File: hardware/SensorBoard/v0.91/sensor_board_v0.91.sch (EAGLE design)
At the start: 46 parts, among them IC1 BMP280, IC2 VREF, J3 USB-MICROB, U1 LMP91000, U10 CCS811, U11 RFM69HW, U2 TSL2561, U3 ATMEGA328P-MU, U4 ADS1115, U7 SHT31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

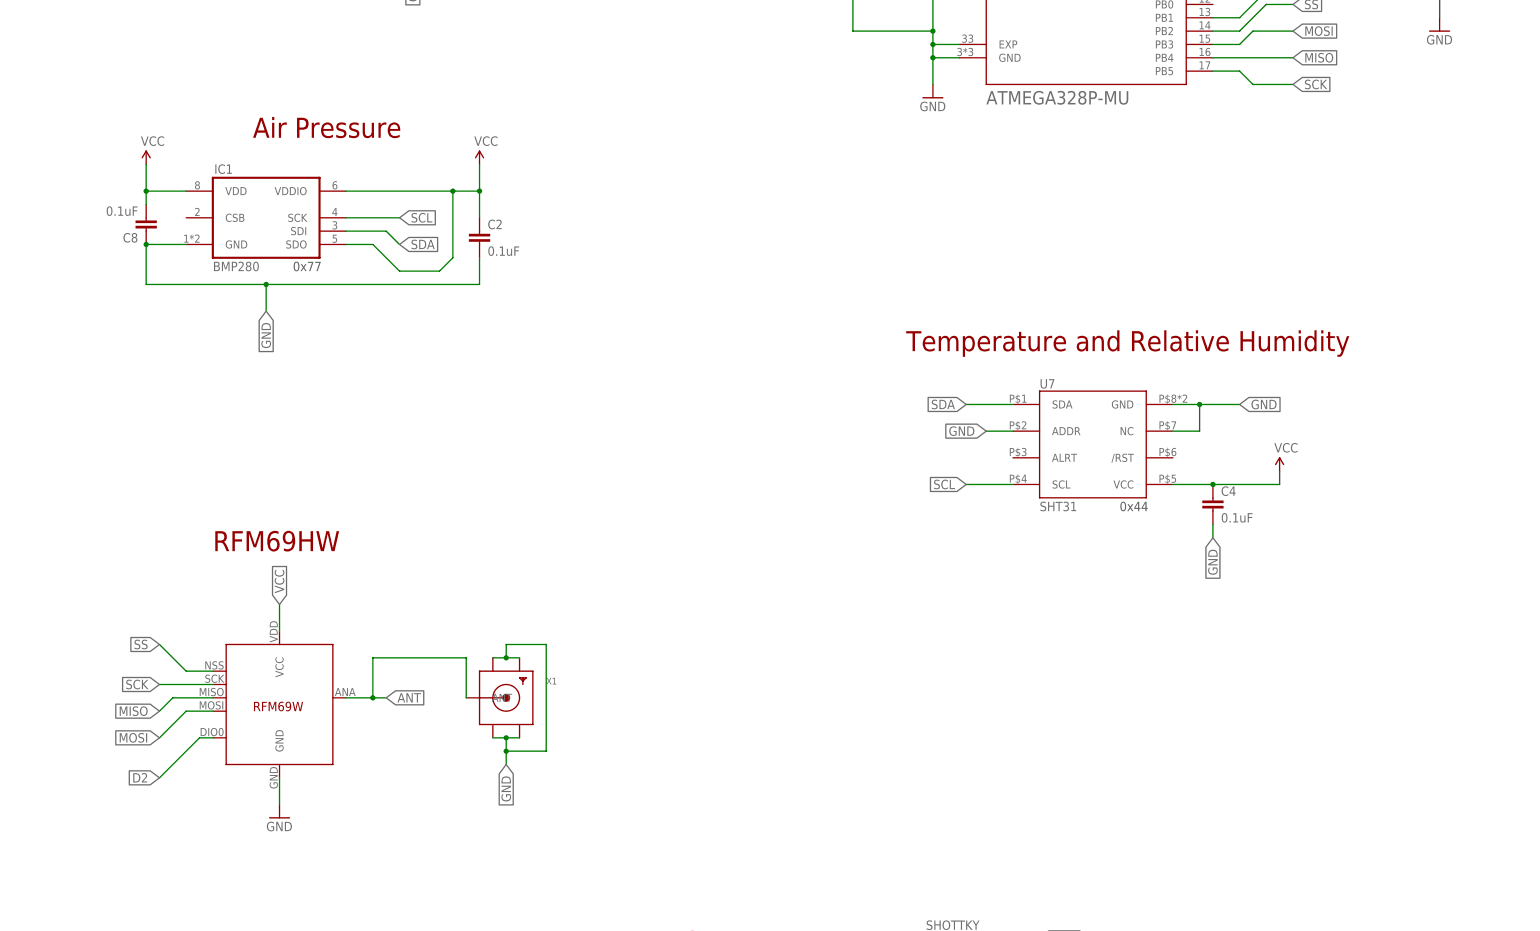
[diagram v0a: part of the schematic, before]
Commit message: Updated SHT31 library
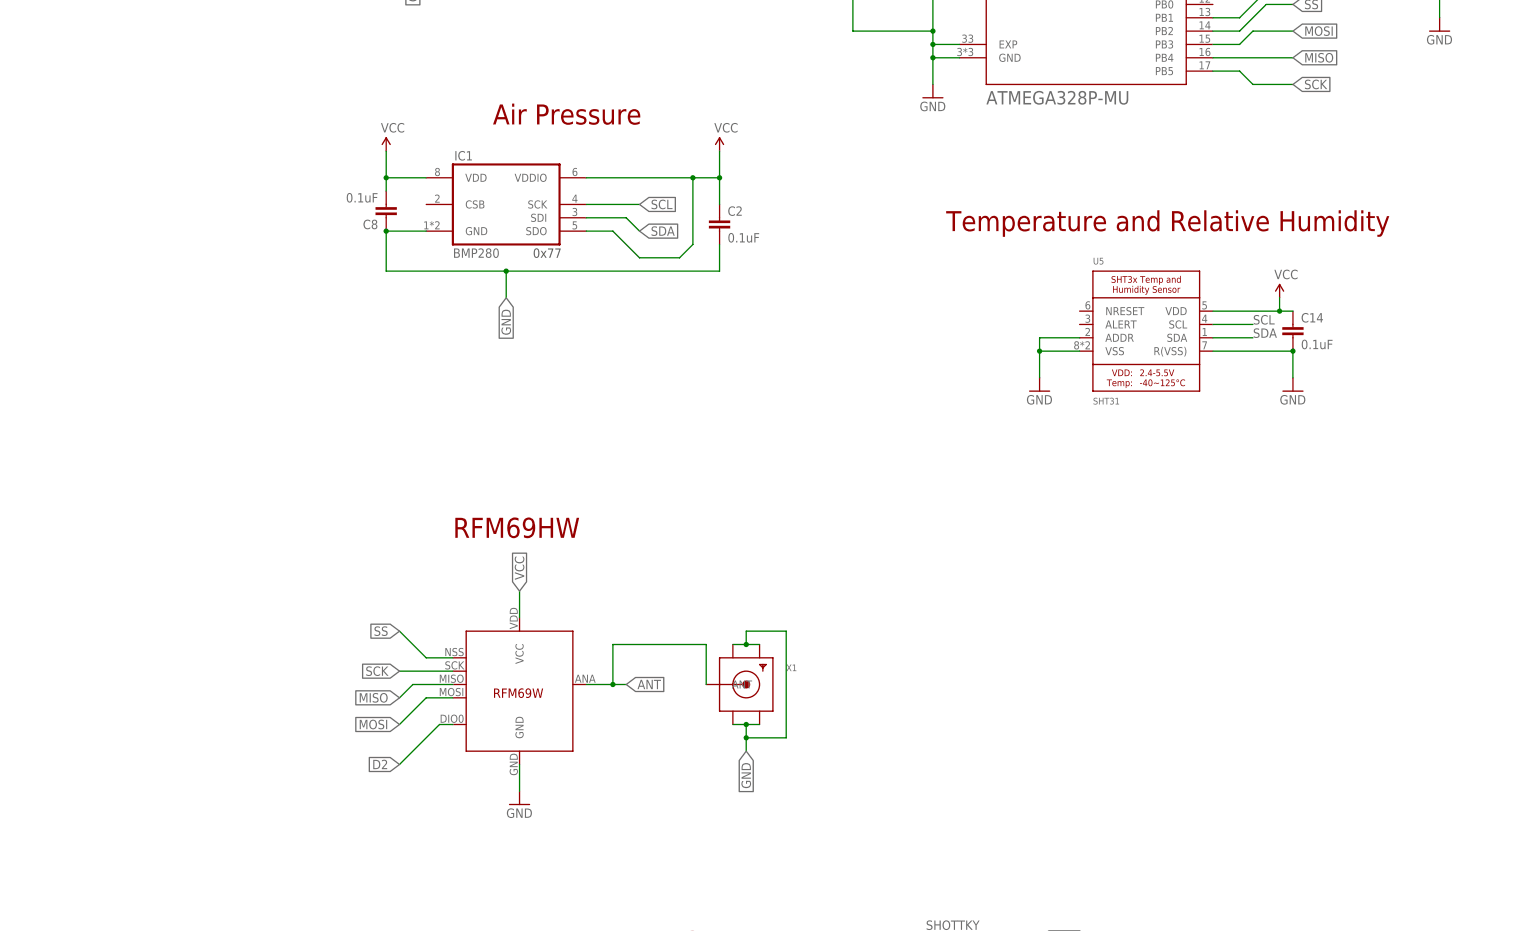
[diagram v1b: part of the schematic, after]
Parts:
- removed C4: 0.1uF, SparkFun-Passives:CAP0805
- removed U7: SHT31, thomasb9511:SHT31-DIS
- added C14: 0.1uF, SparkFun-Passives:CAP0805
- added U5: SHT31, SHT31:SHT3X
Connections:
- net GND: now also C14.2, U5.ADDR, U5.R(VSS), U5.VSS; no longer C4.2, U7.ADDR, U7.GND, U7.NC
- net SCL: now also U5.SCL; no longer U7.SCL
- net SDA: now also U5.SDA; no longer U7.SDA
- net VCC: now also C14.1, U5.VDD; no longer C4.1, U7.VCC
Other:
- note removed: "0x44"
- moved on the sheet: C2, C8, IC1, X1

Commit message: Design update
Replaced TSL2561 with TSL2591 sensor
Rearranged a few traces around the CCS811 sensor
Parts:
- removed C3: 0.1uF, SparkFun-Passives:CAP0805
- removed U2: TSL2561, SparkFun-DigitalIC:TSL2561FN
- added C4: 0.1uF, SparkFun-Passives:CAP0805
- added U6: TSL2591, TSL2591:LIGHT_TSL2591
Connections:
- net GND: now also C4.2, U6.GND; no longer C3.2, U2.GND
- net SCL: now also U6.SCL; no longer U2.SCL
- net SDA: now also U6.SDA; no longer U2.SDA
- net VCC: now also C4.1, U6.VDD; no longer C3.1, U2.VDD
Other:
- note removed: "0x39"
- moved on the sheet: C1, C10, C13, C2, C6, C7, C8, C9, IC1, IC2, R1, R3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
